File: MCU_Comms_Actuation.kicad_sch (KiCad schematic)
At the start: 42 parts, among them J1 MTSW-105-09-L-S-480, Y1 Crystal

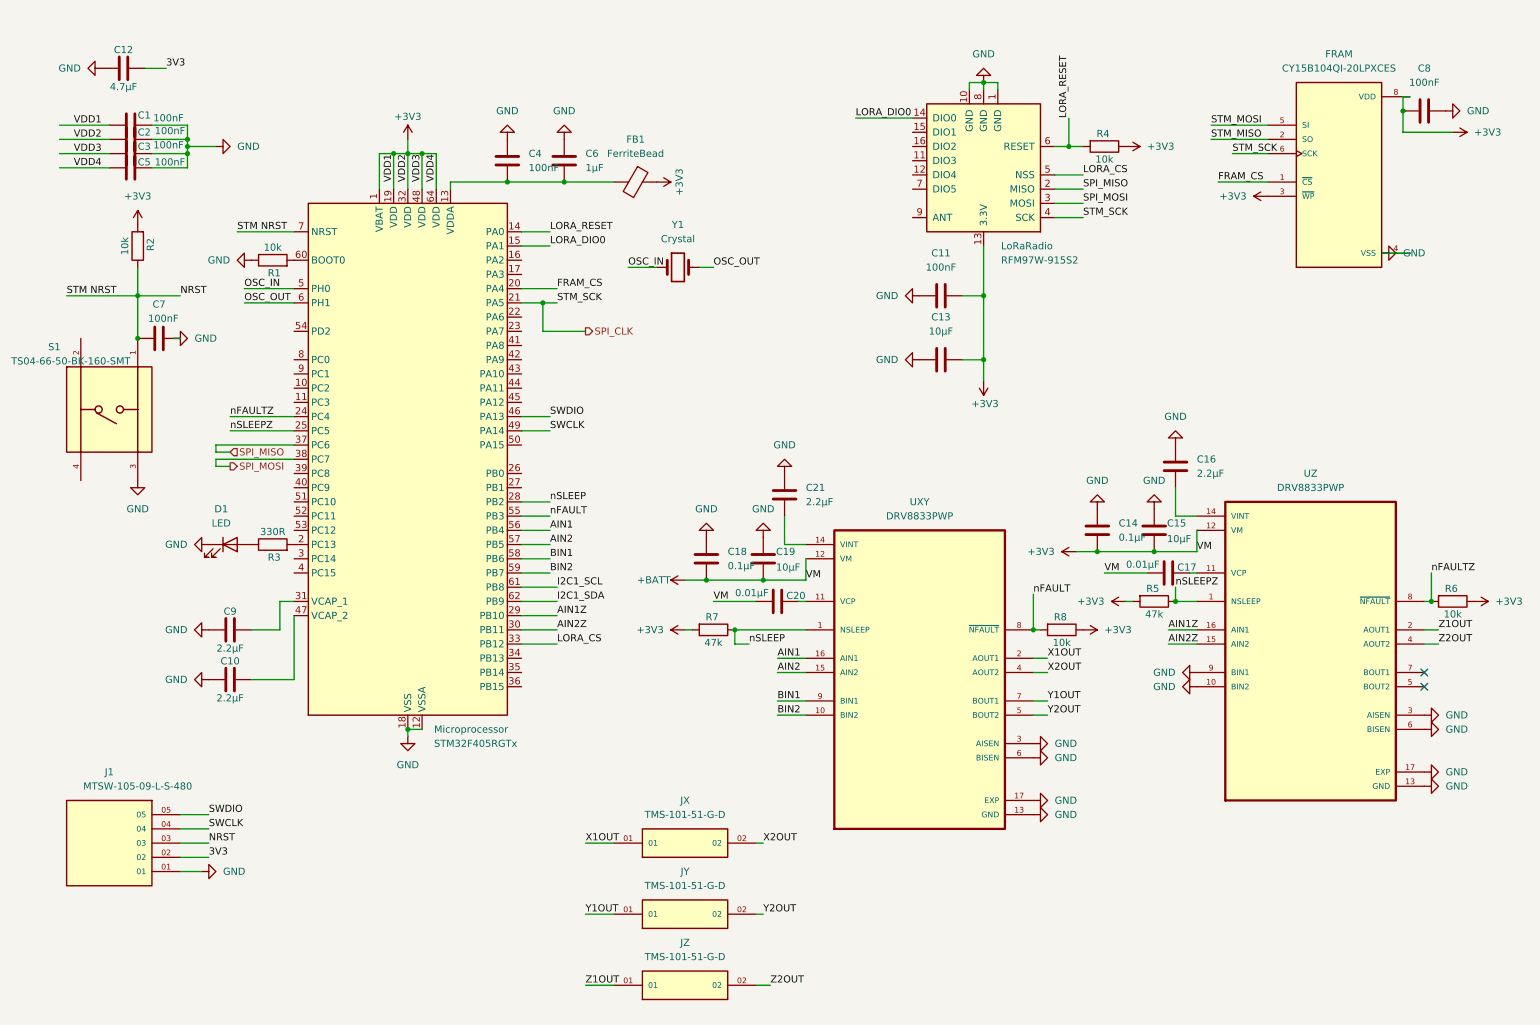
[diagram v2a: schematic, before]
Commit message: Complete STM32 subsystem integration and schematic review
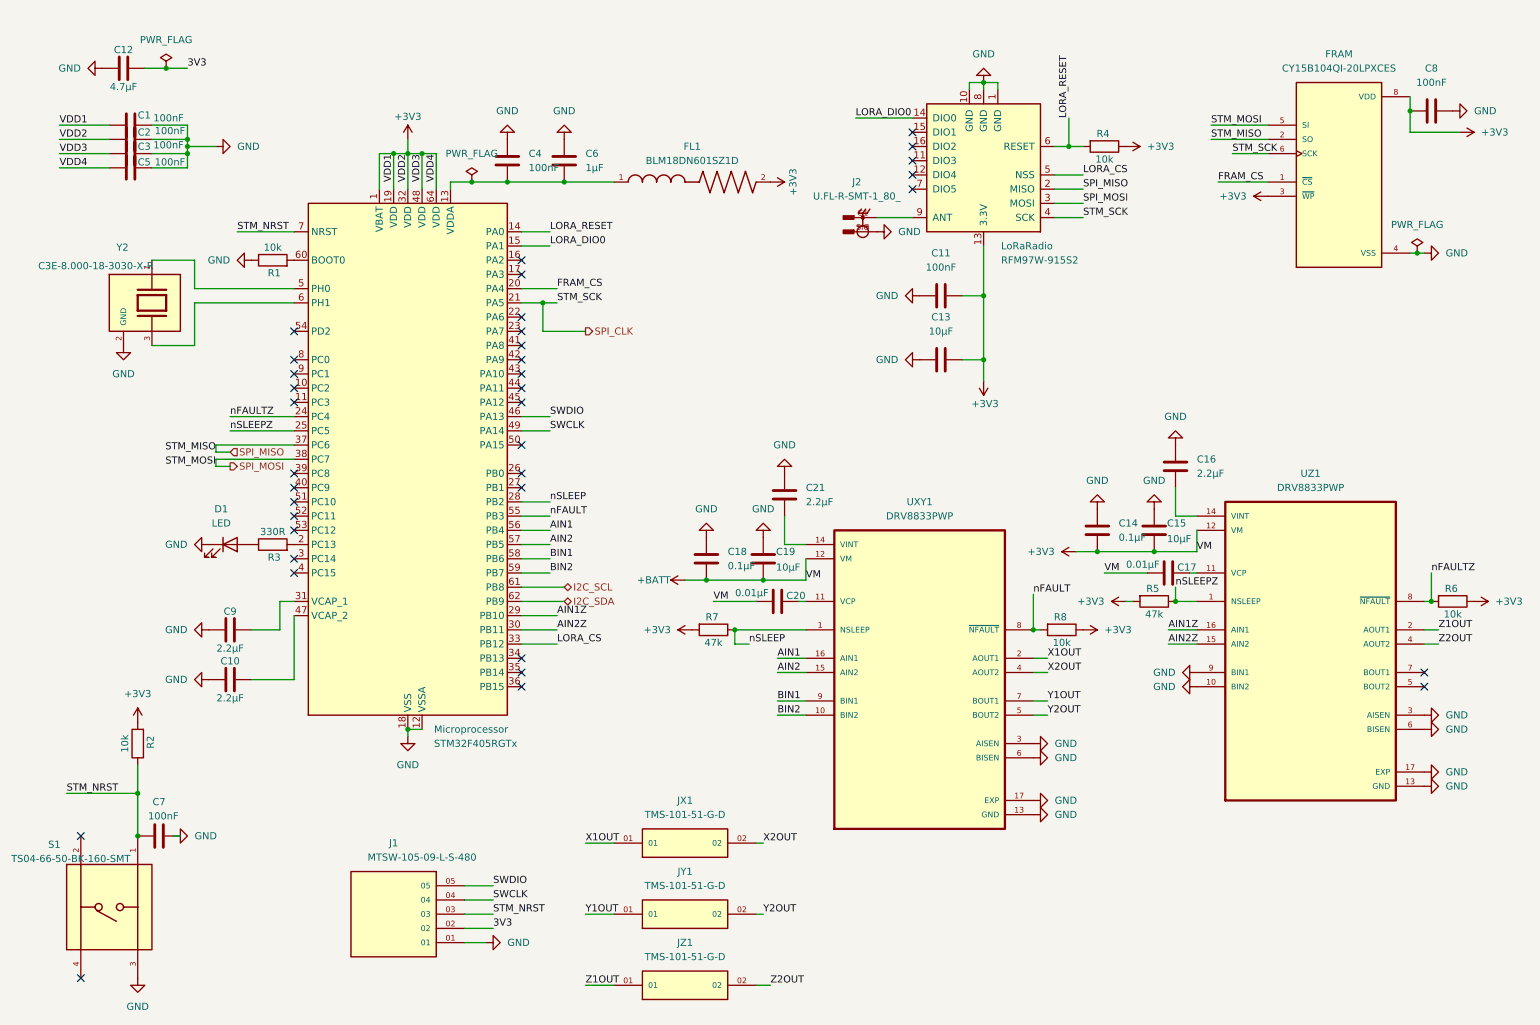
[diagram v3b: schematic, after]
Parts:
- removed FB1: FerriteBead, symbol Device:FerriteBead
- removed Y1: Crystal, symbol Device:Crystal
- added FL1: BLM18DN601SZ1D, BLM18DN601SZ1D:BEADC1608X95N, symbol BLM18DN601SZ1D:BLM18DN601SZ1D
- added J2: U.FL-R-SMT-1_80_, U.FL-R-SMT-1_80_:HIROSE_U.FL-R-SMT-1_80_, symbol U.FL-R-SMT-1_80_:U.FL-R-SMT-1_80_
- added Y2: C3E-8.000-18-3030-X-R, C3E-8.000-18-3030-X-R:XTAL_C3E-8.000-18-3030-X-R, symbol C3E-8.000-18-3030-X-R:C3E-8.000-18-3030-X-R
- C1, C10, C11, C14, C16, C17, C18, C2, C20, C21, C3, C4, C5, C6, C7, C8, C9: footprint (none) -> Capacitor_SMD:C_0603_1608Metric
- C13, C15, C19: footprint (none) -> Capacitor_SMD:C_0805_2012Metric
- R1, R2, R3, R4, R5, R6, R7, R8: footprint (none) -> Resistor_SMD:R_0603_1608Metric
- renumbered JX to JX1, JY to JY1, JZ to JZ1, UXY to UXY1, UZ to UZ1
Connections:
- net STM_MISO is gone; now on net SPI_MISO: FRAM.2 (SO)
- net STM_MOSI is gone; now on net SPI_MOSI: FRAM.5 (SI)
- net +3V3: now also FL1.2
- net GND: now also J2.SIG, Y2.2 (GND), Y2.4 (GND)
- net at C4.2, C6.2, Microprocessor.13 (VDDA): now also FL1.1
- net at LoRaRadio.9 (ANT): now also J2.G1, J2.G2
- net I2C1_SCL renamed I2C_SCL
- net I2C1_SDA renamed I2C_SDA
- net NRST renamed STM_NRST
- net OSC_IN: no longer names the net of Microprocessor.5 (PH0)
- net OSC_IN: now also Y2.1
- net OSC_OUT: no longer names the net of Microprocessor.6 (PH1)
- net OSC_OUT: now also Y2.3
- no-connect marks 2 -> 36
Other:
- moved on the sheet: C7, C8, J1, R2, S1

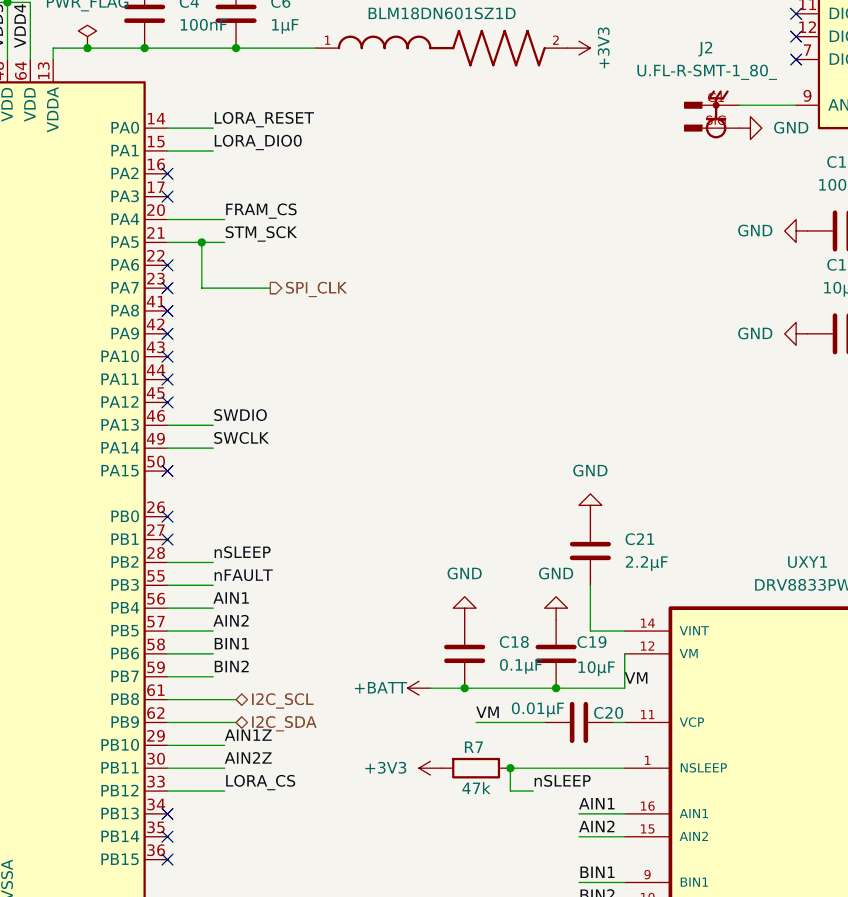
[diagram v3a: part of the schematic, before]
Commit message: Updated GPS, BMI, LSM, and BNO on sensors. Added hierachical labels and new "golden rule" connections
Updated each sensor ensuring they followed the golden rule. I also added hiearchical labels to the topsheet and the inside sheets. Fixed specific sensors to be in SPI vs I2C mode and updated the names.
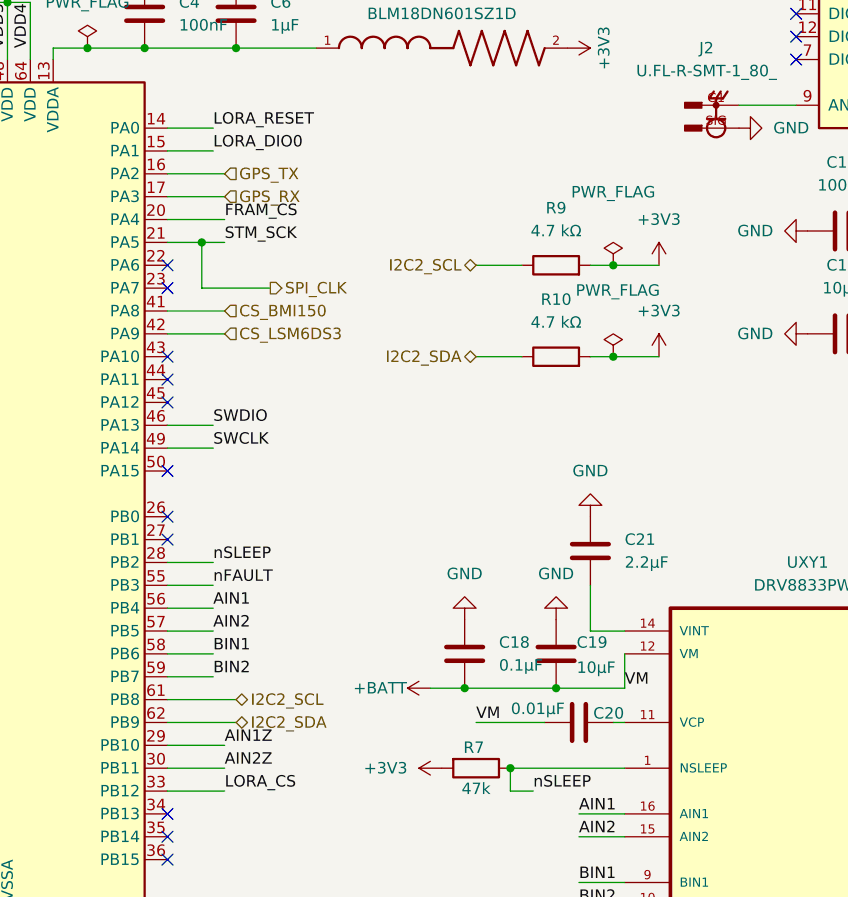
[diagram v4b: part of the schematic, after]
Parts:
- added R10, R9: 4.7 kΩ, symbol Device:R
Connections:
- net +3V3: now also R10.2, R9.2
- net GPS_TX: now reaches Microprocessor.16 (PA2)
- net GPS_RX: now reaches Microprocessor.17 (PA3)
- net CS_BMI150: now reaches Microprocessor.41 (PA8)
- net CS_LSM6DS3: now reaches Microprocessor.42 (PA9)
- net I2C_SCL renamed I2C2_SCL
- net I2C2_SCL: now also R9.1
- net I2C_SDA renamed I2C2_SDA
- net I2C2_SDA: now also R10.1
- no-connect marks 36 -> 32

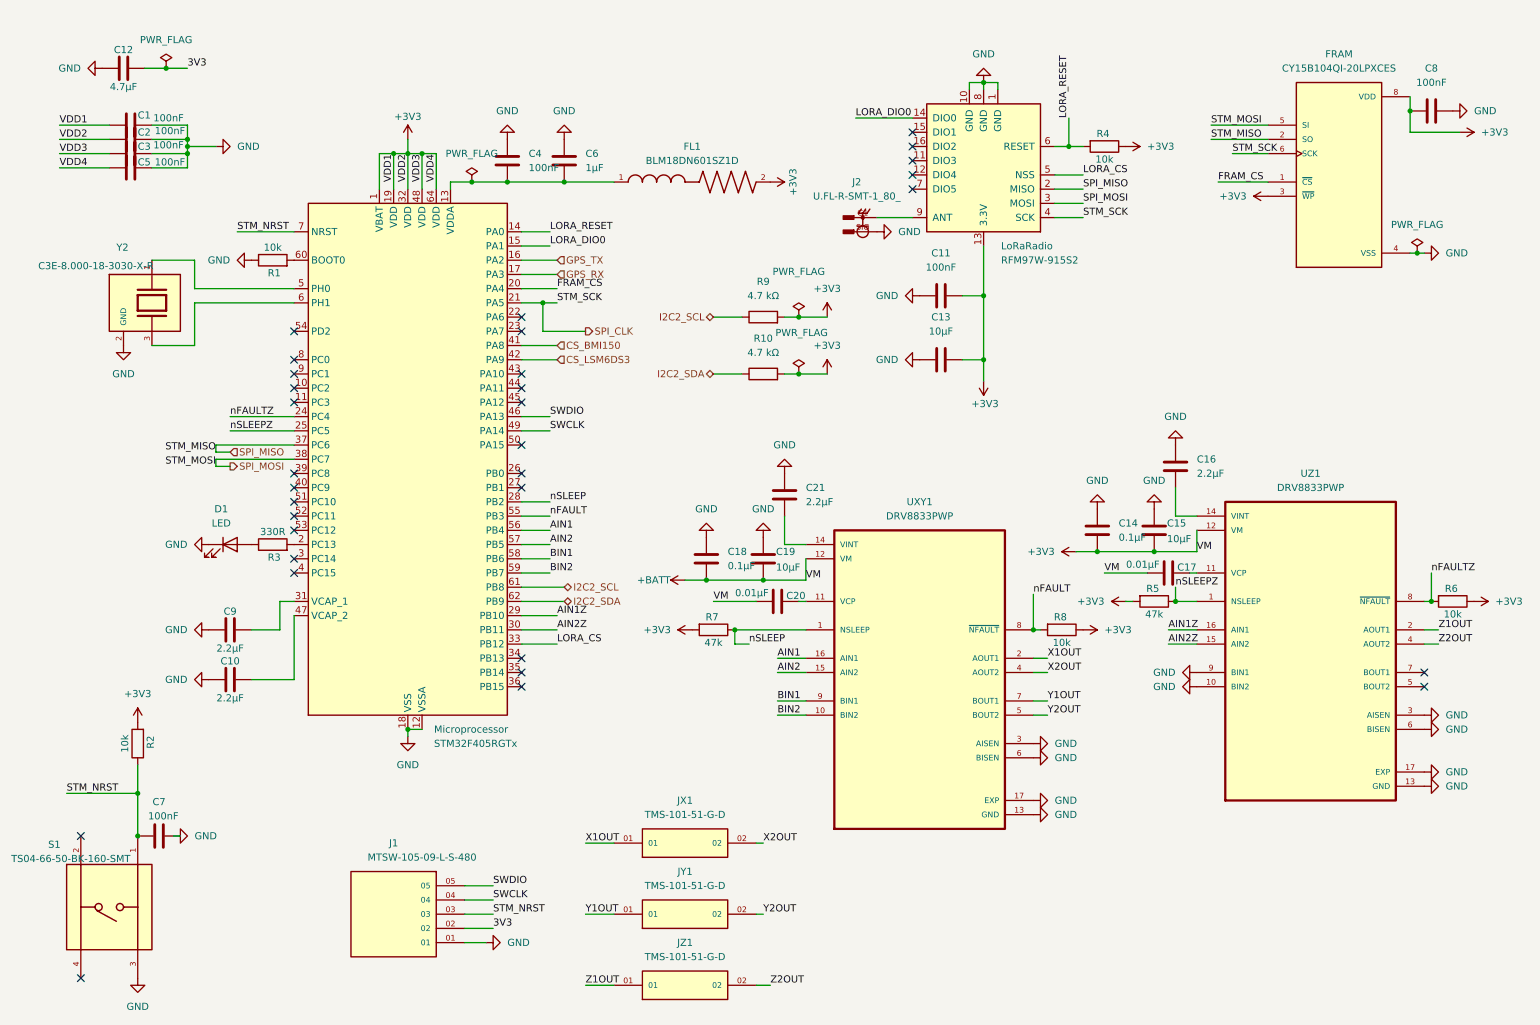
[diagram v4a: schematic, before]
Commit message: Add load switch for sleep rail and IMU interrupt
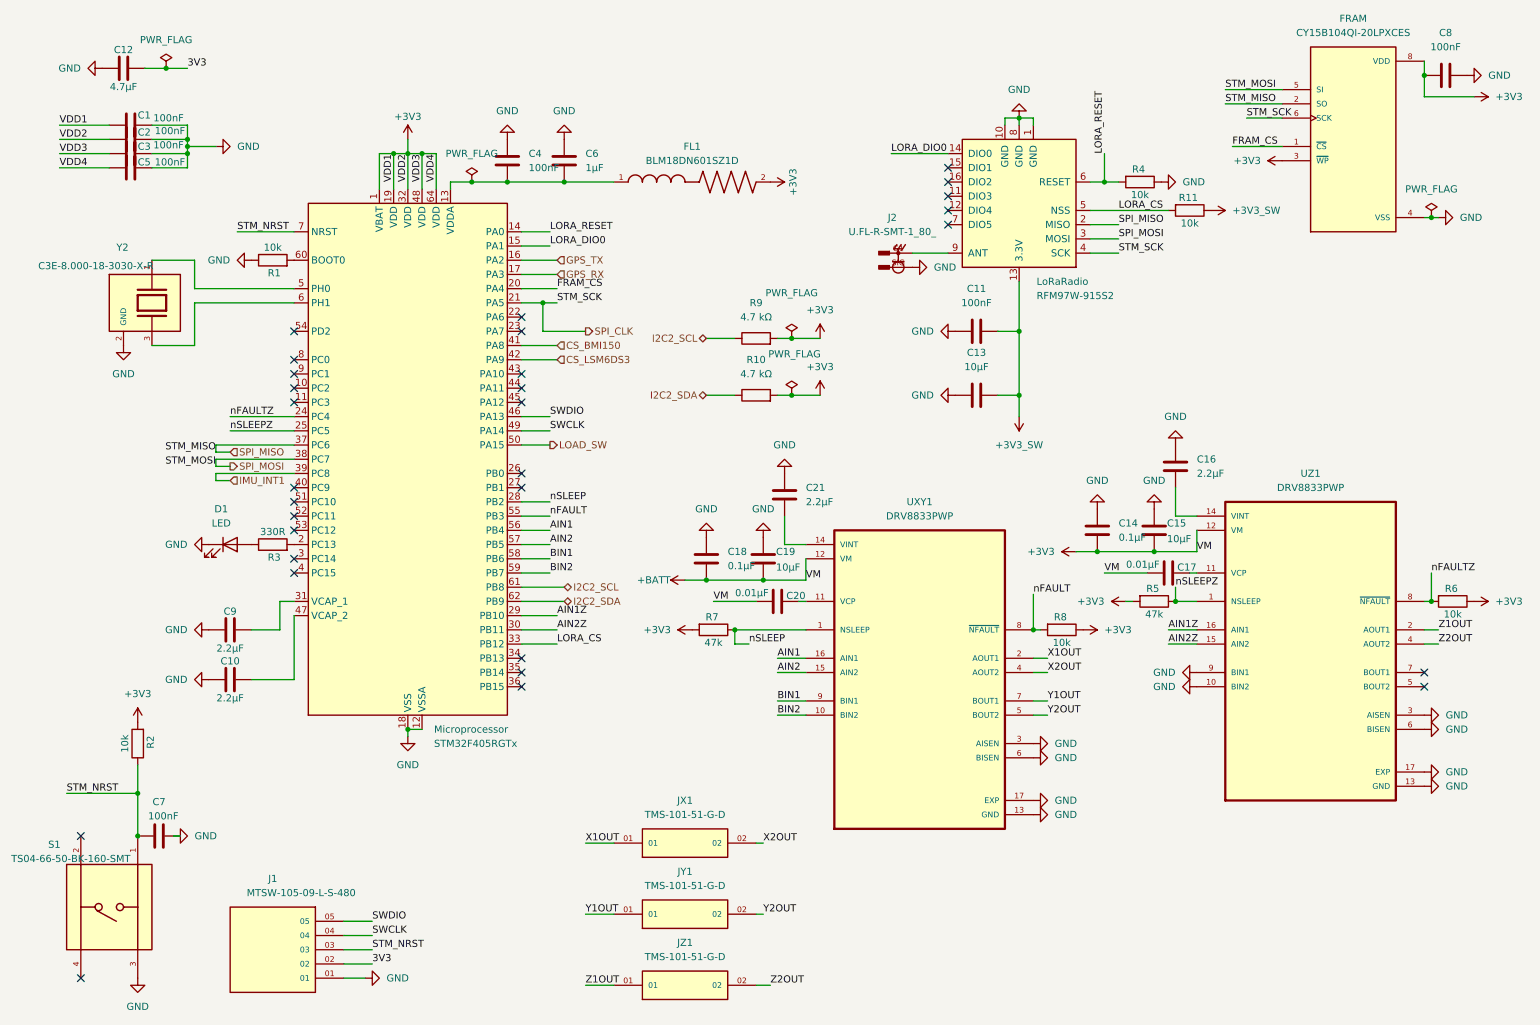
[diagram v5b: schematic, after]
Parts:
- added R11: 10k, Resistor_SMD:R_0603_1608Metric, symbol Device:R
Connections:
- net +3V3: no longer C11.2, C13.2, LoRaRadio.13 (3.3V), R4.1
- net GND: now also R4.1
- net LORA_CS: now also R11.2
- net IMU_INT1: now reaches Microprocessor.39 (PC8)
- net LOAD_SW: now reaches Microprocessor.50 (PA15)
- new net +3V3_SW: C11.2, C13.2, LoRaRadio.13 (3.3V), R11.1
- no-connect marks 32 -> 30
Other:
- moved on the sheet: C11, C13, C8, FRAM, J1, J2, LoRaRadio, R10, R4, R9
